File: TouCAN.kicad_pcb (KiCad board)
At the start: 2 copper layers, 112 x 72 mm, 105 parts, among them J1 m12_M_CAN_90, J10 Conn_01x04, J11 Conn_01x03, J2 USB4105GFA060, J3 DTF13-3P, J4 m12_M_CAN_90, J5 Conn_01x03, J7 DTF13-3P, J8 Conn_01x04, J9 USB_A_Stacked, Q1 PMOS, Q3 PMOS, SW1 OS102011MA1QN1, SW3 OS102011MA1QN1, U1 STM32G431C6Tx, U2 USB2514B_Bi, U3 ADM3053, U5 STM32G431C6Tx, U6 ADM3053, U7 RS3236-3.3YF5, Y1 24mhz

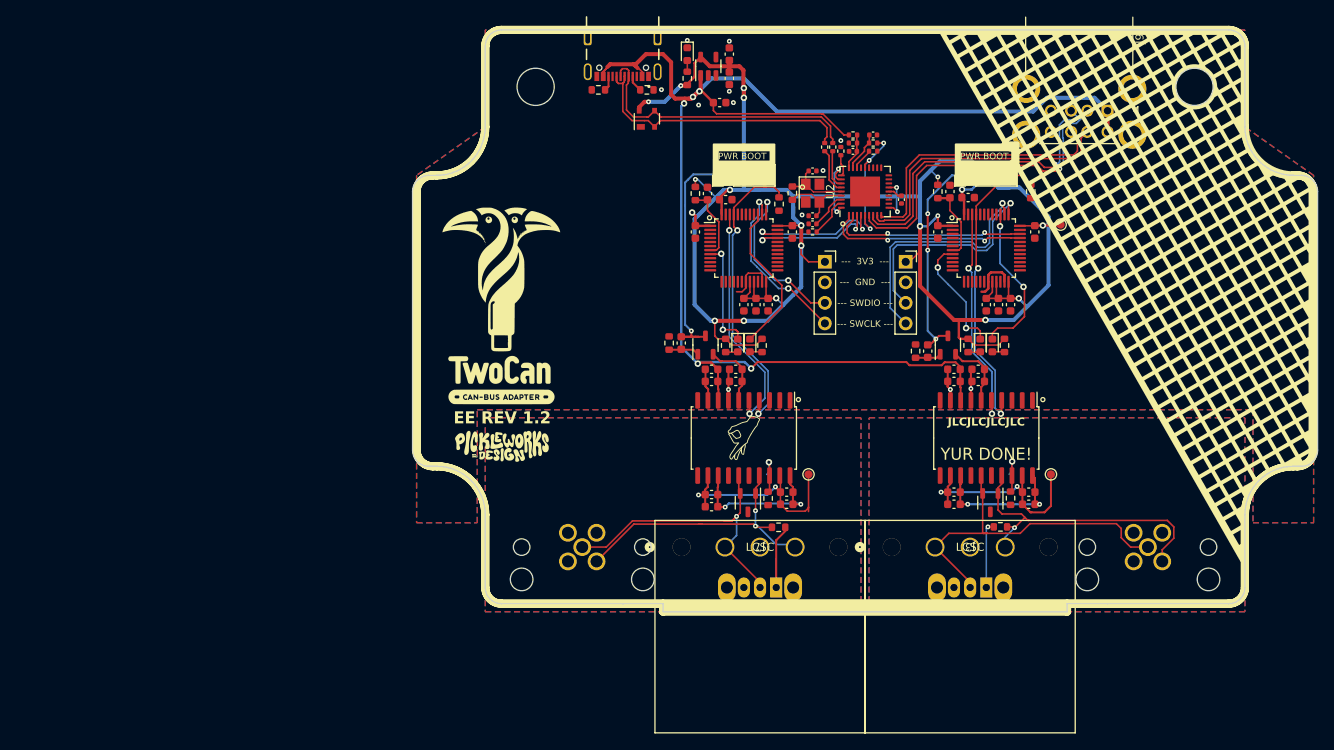
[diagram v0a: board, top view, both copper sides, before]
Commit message: major changes removed m12 and changed layout
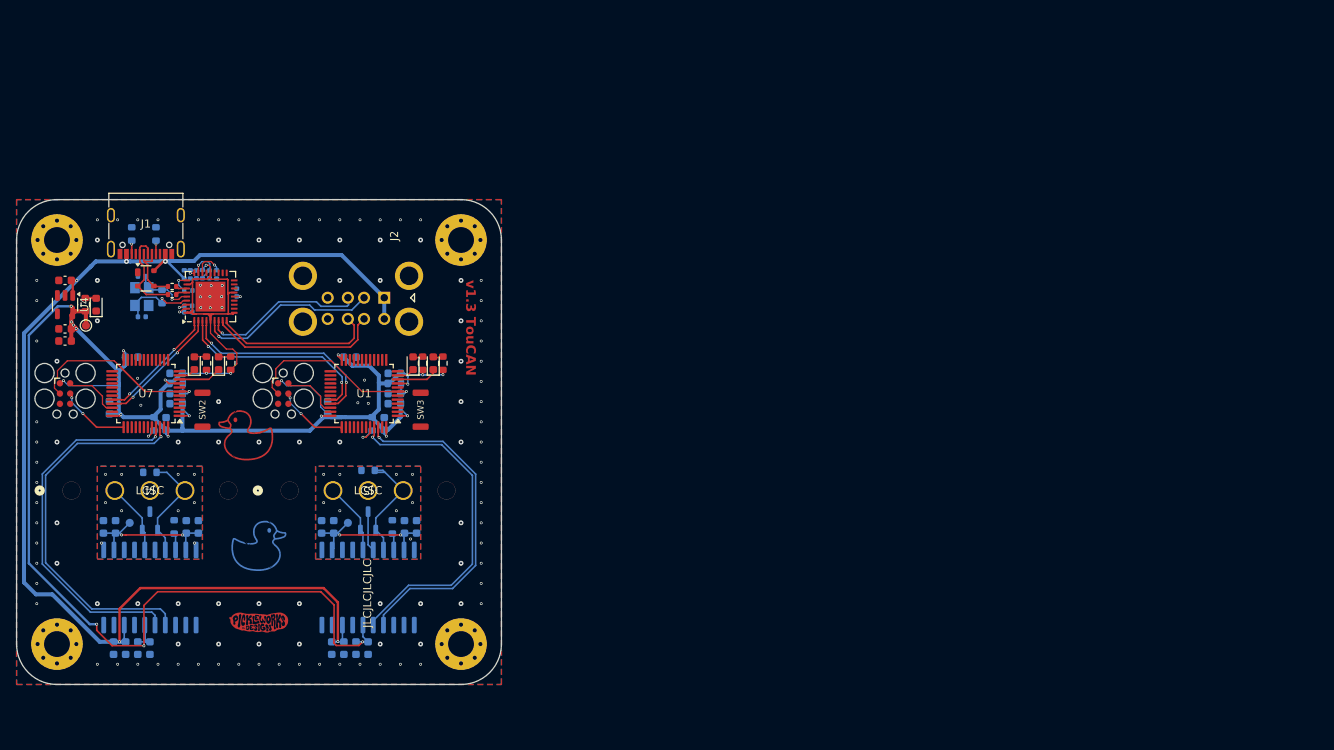
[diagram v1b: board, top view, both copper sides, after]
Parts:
- removed C18, C20, C22, C24, C26, C37, C38, C40, C41: 100nf, Capacitor_SMD:C_0603_1608Metric
- removed C19, C23: 10uf, Capacitor_SMD:C_0603_1608Metric
- removed C21, C25: 10nf, Capacitor_SMD:C_0603_1608Metric
- removed C27, C28, C29, C30, C31: 22uf, Capacitor_SMD:C_0603_1608Metric
- removed D5, D6: blue, LED_SMD:LED_0603_1608Metric
- removed D7: green, LED_SMD:LED_0603_1608Metric
- removed the G*** at (110.0, 59.5)
- removed the G*** at (110.0, 72.0)
- removed the G*** at (139.6, 79.4)
- removed the G*** at (110.0, 80.5)
- removed the G*** at (181.0, 65.0)
- removed J10, J8: Conn_01x04, Connector_PinSocket_2.54mm:PinSocket_1x04_P2.54mm_Vertical
- removed J11: Conn_01x03, Connector_PinHeader_2.54mm:PinHeader_1x03_P2.54mm_Vertical
- removed J7: DTF13-3P, Ethan_footprints:DTF13-3P
- removed J9: USB_A_Stacked, Connector_USB:USB_A_CUI_UJ2-ADH-TH_Horizontal_Stacked
- removed Q1, Q3: PMOS, Ethan_footprints:PMV48XP
- removed R16, R17, R18, R19: 10k, Resistor_SMD:R_0603_1608Metric
- removed R25, R26: 100k, Resistor_SMD:R_0603_1608Metric
- removed the REF** at (155.0, 65.0)
- removed SW1: OS102011MA1QN1, Ethan_footprints:OS102011MA1QN1
- removed TP2: testpad, TestPoint:TestPoint_Pad_D1.0mm
- removed U5: STM32G431C6Tx, Package_QFP:LQFP-48_7x7mm_P0.5mm
- removed U6: ADM3053, Package_SO:SOIC-20W_7.5x12.8mm_P1.27mm
- added ?: , clipboard:af4c8d2e-6e3c-4016-b70e-df9501a44249, F.Cu at (80.1, 102.3)
- added C42: 22uf, Capacitor_SMD:C_0603_1608Metric, B.Cu at (68.5, 77.8)
- added C43: 22uf, Capacitor_SMD:C_0603_1608Metric, B.Cu at (69.8, 75.2)
- added C44: 22uf, Capacitor_SMD:C_0603_1608Metric, B.Cu at (69.8, 71.5)
- added C45: 22uf, Capacitor_SMD:C_0603_1608Metric, B.Cu at (64.2, 69.5)
- added C46: 22uf, Capacitor_SMD:C_0603_1608Metric, B.Cu at (61.5, 75.8)
- added C48: 100nf, Capacitor_SMD:C_0603_1608Metric, B.Cu at (69.8, 74.0)
- added C49: 10uf, Capacitor_SMD:C_0603_1608Metric, B.Cu at (90.5, 105.5)
- added C50: 100nf, Capacitor_SMD:C_0603_1608Metric, B.Cu at (89.0, 105.5)
- added C51: 10nf, Capacitor_SMD:C_0603_1608Metric, B.Cu at (93.5, 105.5)
- added C52: 100nf, Capacitor_SMD:C_0603_1608Metric, B.Cu at (92.0, 105.5)
- added C53: 10uf, Capacitor_SMD:C_0603_1608Metric, B.Cu at (71.0, 90.5)
- added C54: 100nf, Capacitor_SMD:C_0603_1608Metric, B.Cu at (72.5, 90.5)
- added C55: 10nf, Capacitor_SMD:C_0603_1608Metric, B.Cu at (60.8, 90.5)
- added C56: 100nf, Capacitor_SMD:C_0603_1608Metric, B.Cu at (62.2, 90.5)
- added D10: blue, LED_SMD:LED_0603_1608Metric, F.Cu at (72.0, 70.2)
- added D11: ESDA6V1L, Package_TO_SOT_SMD:SOT-23-3, B.Cu at (66.5, 89.8)
- added D9: green, LED_SMD:LED_0603_1608Metric, F.Cu at (75.0, 70.2)
- added G***: LOGO, Projects:duck, F.Cu at (78.4, 79.2)
- added G***: LOGO, Projects:duck, B.Cu at (80.0, 92.8)
- added J6: Conn_ARM_SWD_TagConnect_TC2030, Connector:Tag-Connect_TC2030-IDC-FP_2x03_P1.27mm_Vertical, F.Cu at (56.0, 74.0)
- added R27: 1k, Resistor_SMD:R_0603_1608Metric, B.Cu at (67.0, 77.8)
- added R28: 1k, Resistor_SMD:R_0603_1608Metric, B.Cu at (69.8, 72.8)
- added R32: 10r, Resistor_SMD:R_0603_1608Metric, B.Cu at (69.5, 90.5)
- added R33: 120r, Resistor_SMD:R_0603_1608Metric, B.Cu at (66.5, 83.8)
- added REF**: MountingHole_3.2mm_M3_Pad_Via, MountingHole:MountingHole_3.2mm_M3_Pad_Via, F.Cu at (55.0, 55.0)
- added REF**: MountingHole_3.2mm_M3_Pad_Via, MountingHole:MountingHole_3.2mm_M3_Pad_Via, F.Cu at (105.0, 105.0)
- added REF**: MountingHole_3.2mm_M3_Pad_Via, MountingHole:MountingHole_3.2mm_M3_Pad_Via, F.Cu at (105.0, 55.0)
- added REF**: MountingHole_3.2mm_M3_Pad_Via, MountingHole:MountingHole_3.2mm_M3_Pad_Via, F.Cu at (55.0, 105.0)
- added SW2: smol_button, pickle_parts:smol_button, F.Cu at (73.0, 76.0)
- added TP7: testpad, TestPoint:TestPoint_Pad_D1.0mm, B.Cu at (64.0, 90.0)
- added U4: RS3236-3.3YF5, Package_TO_SOT_SMD:SOT-23-5, F.Cu at (56.0, 63.0)
- added U8: ADM3053, Package_SO:SOIC-20W_7.5x12.8mm_P1.27mm, B.Cu at (66.5, 98.0)
- C1: value 100nf -> 22uf; moved to B.Cu
- C10: value 100nf -> 10uf; moved to B.Cu
- C11, C12, C14, C15, C16, C17, C2, C3, C32, C33, C4, C5, D2, R13, R14, R15, R20, R22, R3, R4, TP3, U3, Y1: moved to B.Cu
- C13: value 10uf -> 100nf; moved to B.Cu
- C34, C35: value 18pF -> 100nF; moved to B.Cu
- C36, C39: value 100nF -> 18pF; moved to B.Cu
- C6: value 22uf -> 100nf; moved to B.Cu
- D1: value ESDA6V1L -> green; footprint Package_TO_SOT_SMD:SOT-23-3 -> LED_SMD:LED_0603_1608Metric
- D3: value PRTR5V0U2X -> red; footprint Package_TO_SOT_SMD:SOT-143 -> LED_SMD:LED_0603_1608Metric
- D4: value green -> blue
- D8: value red -> PRTR5V0U2X; footprint LED_SMD:LED_0603_1608Metric -> Package_TO_SOT_SMD:SOT-143
- J1: value m12_M_CAN_90 -> USB4105GFA060; footprint Ethan_footprints:M12A-05PMMR-EE0001 -> pickle_parts:USB_C_Receptacle_G-Switch_GT-USB-7010ASV_pickle
- J2: value USB4105GFA060 -> USB_A_Stacked; footprint Ethan_footprints:GCT_USB4105GFA060 -> Connector_USB:USB_A_CUI_UJ2-ADH-TH_Horizontal_Stacked
- J3: value DTF13-3P -> Conn_ARM_SWD_TagConnect_TC2030; footprint Ethan_footprints:DTF13-3P -> Connector:Tag-Connect_TC2030-IDC-FP_2x03_P1.27mm_Vertical
- J4: value m12_M_CAN_90 -> DTF13-3P; footprint Ethan_footprints:M12A-05PMMR-EE0001 -> pickle_parts:DTF13-3P
- J5: value Conn_01x03 -> DTF13-3P; footprint Connector_PinHeader_2.54mm:PinHeader_1x03_P2.54mm_Vertical -> pickle_parts:DTF13-3P
- R1: value 10r -> 1k; moved to B.Cu
- R12: value 12k -> 100k; moved to B.Cu
- R2: value 120r -> 1k; moved to B.Cu
- R21: value 100k -> 12k; moved to B.Cu
- R5: value 120r -> 10r; moved to B.Cu
- R6: value 10r -> 120r; moved to B.Cu
- SW3: value OS102011MA1QN1 -> smol_button; footprint Ethan_footprints:OS102011MA1QN1 -> pickle_parts:smol_button; moved to F.Cu
- U1: value STM32G431C6Tx -> STM32F072C8Tx
- U7: value RS3236-3.3YF5 -> STM32F072C8Tx; footprint Package_TO_SOT_SMD:SOT-23-5 -> Package_QFP:LQFP-48_7x7mm_P0.5mm
- moved J1 130.3 mm to (66.0, 53.0), turned to 180 degrees
- moved TP1 121.3 mm to (58.6, 65.6), turned to 0 degrees
- moved C11 111.0 mm to (63.5, 105.5), turned to 90 degrees
- moved C10 109.1 mm to (62.0, 105.5), turned to 90 degrees
- moved C12 109.1 mm to (65.0, 105.5), turned to 90 degrees
- moved C13 105.3 mm to (66.5, 105.5), turned to 90 degrees
- moved C36 93.3 mm to (65.5, 64.5), turned to 180 degrees
- moved C8 89.5 mm to (56.0, 67.5), turned to 0 degrees
- moved C9 87.9 mm to (56.0, 66.0), turned to 0 degrees
- moved C32 87.7 mm to (72.2, 59.2)
- moved C16 87.6 mm to (87.8, 90.5), turned to -90 degrees
- moved J3 87.1 mm to (83.0, 74.0), turned to -90 degrees
- moved R15 86.7 mm to (71.2, 61.2), turned to 0 degrees
- moved C17 86.0 mm to (89.2, 90.5), turned to -90 degrees
- moved C3 85.5 mm to (88.5, 75.8), turned to -90 degrees
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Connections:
- C1 pad 1: +3V3 -> GND
- C1 pad 2: GND -> +3V3
- C11 pad 2: 3v3_sw1 -> +5V
- C12 pad 2: 3v3_sw1 -> +3V3
- C13 pad 2: +5V -> +3V3
- C14 pad 1: GND1 -> GND2
- C15 pad 1: GND1 -> GND2
- C16 pad 1: GND1 -> GND2
- C17 pad 1: GND1 -> GND2
- C32 pad 1: Net-(U2-CRFILT) -> /hub/VBUS_DET
- C33 pad 1: VBUS_DET -> Net-(U2-RESET_N)
- C34 pad 1: GND -> Net-(U2-CRFILT)
- C34 pad 2: Net-(U2-XTALIN/CLKIN) -> GND
- C35 pad 1: GND -> Net-(U2-PLLFILT)
- C35 pad 2: Net-(U2-XTALOUT) -> GND
- C36 pad 1: Net-(U2-RESET_N) -> GND
- C36 pad 2: GND -> Net-(U2-XTALIN/CLKIN)
- C39 pad 1: Net-(U2-PLLFILT) -> GND
- C39 pad 2: GND -> Net-(U2-XTALOUT)
- C6 pad 1: GND -> /Brains2/~{RESET}
- C6 pad 2: +3V3 -> GND
- D1 pad 1: 1CAN_+ -> /Brains2/WORD_LED
- D1 pad 2: 1CAN_- -> Net-(D1-A)
- D2 pad 1: 2CAN_+ -> /CAN2/CAN_+
- D2 pad 2: 2CAN_- -> /CAN2/CAN_-
- D3 pad 2: 0USB_+ -> Net-(D3-A)
- D4 pad 1: 1WORD_LED -> /Brains2/STAT_LED
- D8 pad 2: Net-(D8-A) -> /Power/USB_+
- J3 pad 4: (no net) -> /Brains2/SWCLK
- J3 pad 5: (no net) -> GND
- J4 pad 4: 2CAN_+ -> (no net)
- J4 pad 5: 2CAN_- -> (no net)
- R1 pad 1: GND1 -> +3V3
- R1 pad 2: Net-(U3-RS) -> /Brains2/BOOT
- R12 pad 1: Net-(U2-RBIAS) -> +5V
- R12 pad 2: GND -> /hub/VBUS_DET
- R13 pad 1: +5V -> /hub/VBUS_DET
- R13 pad 2: VBUS_DET -> GND
- R14 pad 1: VBUS_DET -> +3V3
- R14 pad 2: GND -> Net-(U2-RESET_N)
- R15 pad 1: +3V3 -> Net-(U2-SUSP_IND/LOCAL_PWR/NON_REM0)
- R15 pad 2: Net-(U2-RESET_N) -> GND
- R2 pad 1: 1CAN_+ -> +3V3
- R2 pad 2: Net-(SW3-A) -> /Brains2/~{RESET}
- R21 pad 1: Net-(U2-SUSP_IND/LOCAL_PWR/NON_REM0) -> Net-(U2-RBIAS)
- R23 pad 2: 0USB_- -> /Power/USB_-
- R24 pad 2: 0USB_+ -> /Power/USB_+
- R3 pad 2: Net-(J2-CC2) -> Net-(J1-CC2)
- R4 pad 2: Net-(J2-CC1) -> Net-(J1-CC1)
- R5 pad 1: 2CAN_+ -> GND2
- R5 pad 2: Net-(SW1-A) (its old number) -> Net-(U3-RS)
- R6 pad 1: GND2 -> /CAN2/CAN_+
- R7 pad 2: Net-(D5-A) -> Net-(D1-A)
- R9 pad 2: Net-(D8-A) -> Net-(D3-A)
- SW3 pad 1: Net-(SW3-A) -> /Brains2/BOOT
- SW3 pad 2: 1CAN_- -> GND
- TP3 pad 1: Net-(U6-VISOIN) -> Net-(U3-VISOIN)
- U1 pad 10: unconnected-(U1-PA2-Pad10) -> /Brains2/WORD_LED
- U1 pad 11: unconnected-(U1-PA3-Pad11) -> /Brains2/STAT_LED
- U1 pad 19: GND -> unconnected-(U1-PB1-Pad19)
- U1 pad 20: +3V3 -> unconnected-(U1-PB2-Pad20)
- U1 pad 21: +3V3 -> unconnected-(U1-PB10-Pad21)
- U1 pad 32: unconnected-(U1-PA10-Pad32) -> /2USB_-
- U1 pad 33: 1USB_- -> /2USB_+
- U1 pad 34: 1USB_+ -> /Brains2/SWDIO
- U1 pad 37: 1SWDIO -> /Brains2/SWCLK
- U1 pad 38: 1SWCLK -> unconnected-(U1-PA15-Pad38)
- U1 pad 39: 1STAT_LED -> unconnected-(U1-PB3-Pad39)
- U1 pad 44: unconnected-(U1-PB7-Pad44) -> /Brains2/BOOT
- U1 pad 45: 1CAN_RX -> /Brains2/CAN_RX
- U1 pad 46: 1CAN_TX -> /Brains2/CAN_TX
- U1 pad 7: 1NRST -> /Brains2/~{RESET}
- U1 pad 8: 1WORD_LED -> GND
- U1 pad 9: unconnected-(U1-PA1-Pad9) -> +3V3
- U2 pad 1: 1USB_- -> /1USB_-
- U2 pad 2: 1USB_+ -> /1USB_+
- U2 pad 27: VBUS_DET -> /hub/VBUS_DET
- U2 pad 3: 2USB_- -> /2USB_-
- U2 pad 4: 2USB_+ -> /2USB_+
- U2 pad 6: 3USB_- -> /hub/3USB_-
- U2 pad 7: 3USB_+ -> /hub/3USB_+
- U2 pad 8: 4USB_- -> /hub/4USB_-
- U2 pad 9: 4USB_+ -> /hub/4USB_+
- U3 pad 11: GND1 -> GND2
- U3 pad 13: GND1 -> GND2
- U3 pad 15: 1CAN_- -> /CAN2/CAN_-
- U3 pad 16: GND1 -> GND2
- U3 pad 17: 1CAN_+ -> /CAN2/CAN_+
- U3 pad 20: GND1 -> GND2
- U3 pad 4: 1CAN_RX -> /Brains2/CAN_TX
- U3 pad 5: 1CAN_TX -> /Brains2/CAN_RX
- U3 pad 6: 3v3_sw1 -> +3V3
- U7 pad 1: +5V -> +3V3
- U7 pad 2: GND -> unconnected-(U7-PC13-Pad2)
- U7 pad 3: (no net) -> unconnected-(U7-PC14-Pad3)
- U7 pad 4: (no net) -> unconnected-(U7-PC15-Pad4)
- U7 pad 5: +3V3 -> unconnected-(U7-PF0-Pad5)
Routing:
- net /Brains/CAN_TX: track 0.00 -> 47.1 mm, vias 0 -> 1
- net /Brains/CAN_RX: track 0.00 -> 46.0 mm, vias 0 -> 1
- net 1CAN_-: track 44.7 -> 0.00 mm
- net /Brains2/CAN_RX: track 0.00 -> 42.3 mm, vias 0 -> 1
- net /Brains2/CAN_TX: track 0.00 -> 41.6 mm, vias 0 -> 1
- net 3USB_-: track 40.7 -> 0.00 mm, vias 1 -> 0
- net 2CAN_RX: track 40.5 -> 0.00 mm, vias 2 -> 0
- net 2CAN_-: track 39.6 -> 0.00 mm, vias 1 -> 0
- net 3USB_+: track 39.2 -> 0.00 mm, vias 1 -> 0
- net 1CAN_+: track 38.8 -> 0.00 mm, vias 1 -> 0
- net 1CAN_RX: track 37.8 -> 0.00 mm, vias 2 -> 0
- net 2CAN_+: track 37.3 -> 0.00 mm, vias 2 -> 0
- net 0USB_-: track 35.7 -> 0.00 mm
- net 4USB_-: track 35.4 -> 0.00 mm
- net 0USB_+: track 34.9 -> 0.00 mm
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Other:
- board size 112 x 72 mm -> 60 x 60 mm
- board text added: "v1.3 TouCAN"
- board text removed: "--- 3V3 --- --- GND --- --- SWDIO --- --- SWCLK ---"
- board text removed: "EE REV 1.2"
- board text removed: "PWR BOOT"
- board text removed: "YUR DONE!"
